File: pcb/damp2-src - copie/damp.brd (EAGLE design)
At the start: 73 x 48.9 mm, 24 parts, among them IC2 74C74N, K1 G5L, Q3 BSS138, Q5 BSS138

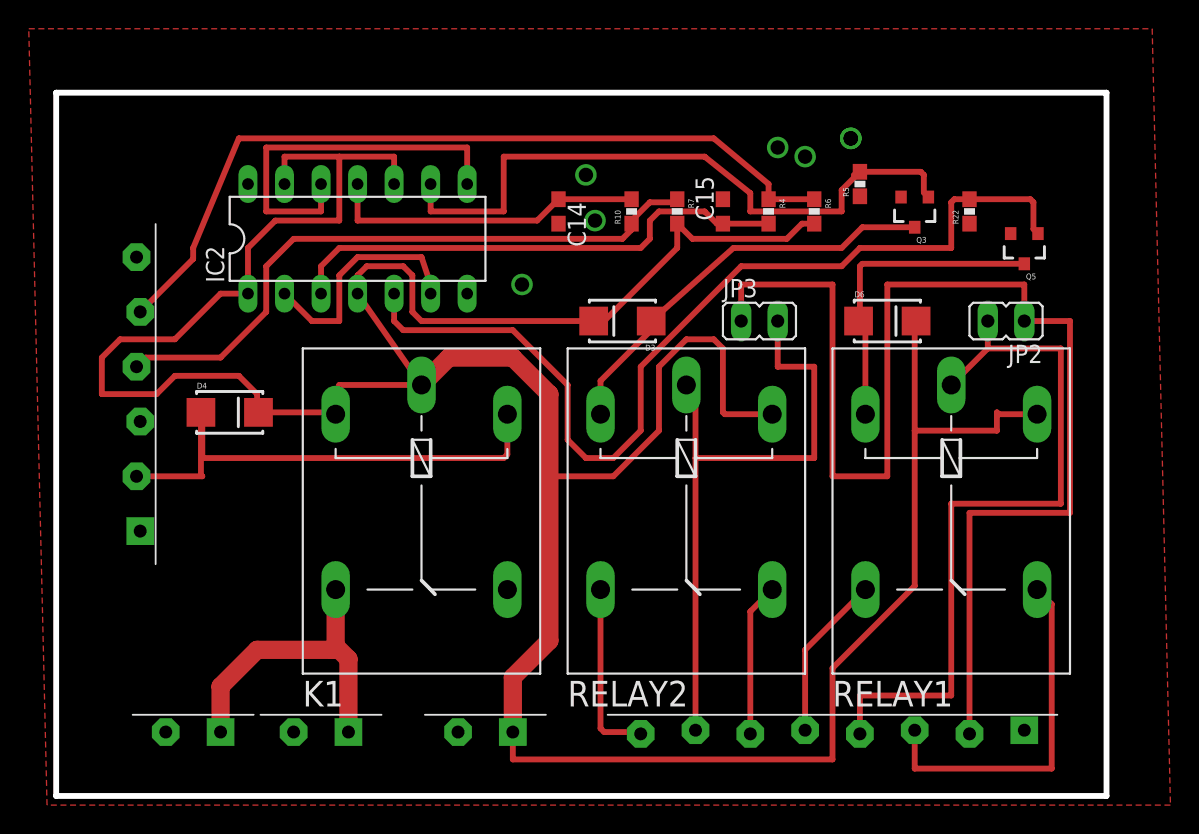
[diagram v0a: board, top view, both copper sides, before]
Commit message: minor debug (hole + value)
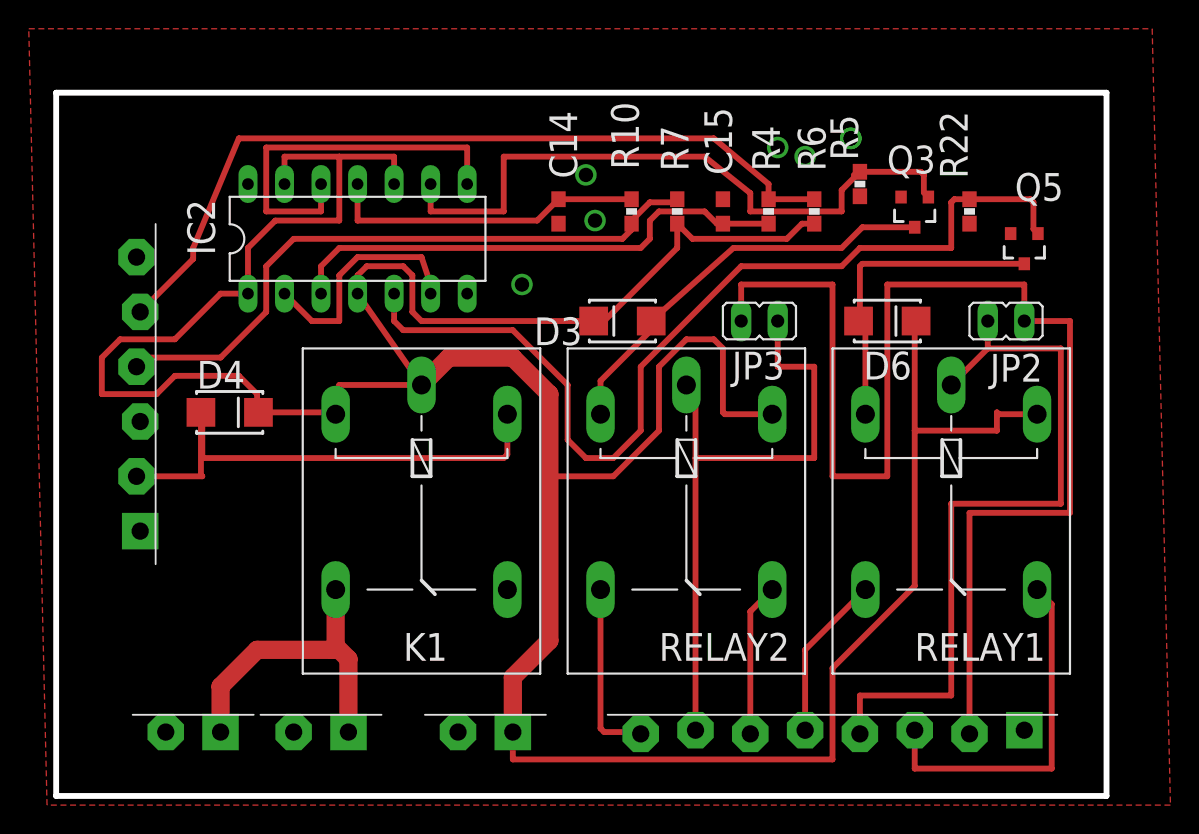
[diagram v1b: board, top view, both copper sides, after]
